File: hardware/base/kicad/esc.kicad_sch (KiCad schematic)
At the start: 69 parts, among them J3 HY911105AE IN, J4 HY911105AE OUT, U4 LAN9253-I/R4X, U5 TPS3808G33DBVR, U6 M24C16-RMN6TP, U7 TPD4E05U06DQAR, U8 TPD4E05U06DQAR

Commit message: Place the base board parts; DIP switches for the encoder terminations
Placement (gen/pcb.py): one zone per schematic sheet, key parts placed by
hand, the other parts next to the pin they serve, bulkiest first, with a
1 mm gap preferred when it costs at most 2 mm. The local bus header stands
at the left end, centred across the board, facing the modules.

Encoder terminations: one CTS 218-4LPSTR DIP switch per encoder (100 mA
non-switching) replaces three SMD jumpers; the supply selector and the
Modbus termination use a through-hole 1x3 header. Split DIP symbol, one
unit per switch, drawn on the pair it serves.

DRC rules: 0.2 mm thermal vias, per-package clearance for 0.65 mm pitch
parts. Test points out of the BOM, DNP copied to the footprints. pcb.py
keeps the schematic settings of the project file and finds the KiCad
footprint libraries on every install.

Claude-Session: https://claude.ai/code/session_01JfmMsHNpEd1mfzHNWc4koJ
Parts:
- TP1, TP2, TP3: now left out of the parts list

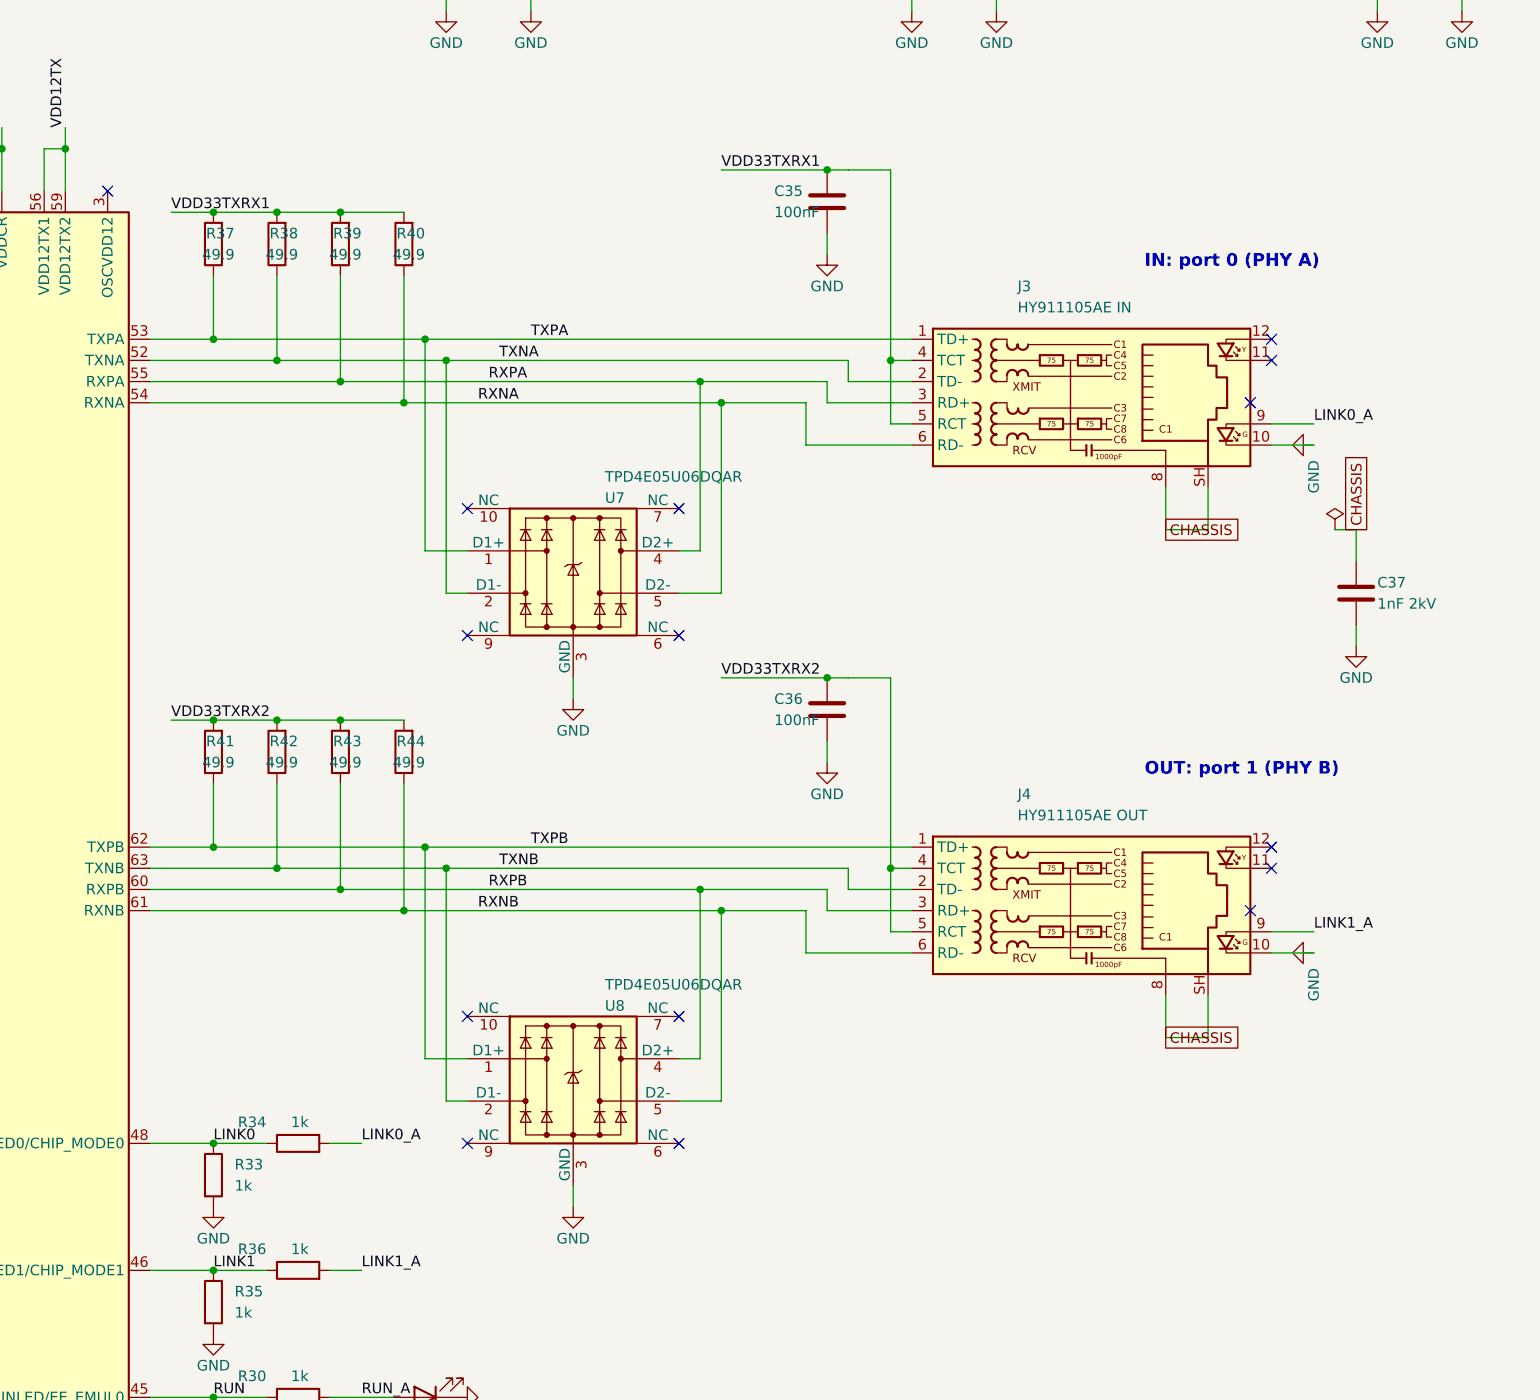
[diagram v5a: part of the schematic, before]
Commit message: Differential pairs routed by script; PHY to jack mapping for a planar layout
- pairs.py, pass "pairs" right after the planes and trunks: A* on a 0.1 mm
  grid for the centre line of each pair, clear of the other copper by about
  3 W (by the clearance alone near the pads), offset into its two lines;
  straight out of the QFN pads, straight through the ESD arrays, each line on
  its own into the through-hole pins of the jack. Ethernet 100 ohm and USB
  90 ohm at 0.15 mm gap (sim/impedance.py).
- Schematic: the lines on the jack pins and ESD channels in the order that
  routes without a crossing (port A with P and N swapped, port B with TX and
  RX swapped: the LAN9253 PHYs correct the polarity and have HP Auto-MDIX);
  the NC pins of the ESD arrays opposite each line carry it (TI flow-through).
- Ethernet terminations lifted off the board while the pairs are routed, then
  put against their line, 2 to 10 mm from the PHY pins; the lines inside a
  port straddled by their 0603 termination (49.9 ohm moved to 0603, C23185,
  basic, 1.78 M in stock on 2026-10-20; clock series resistors too).
- Placement: lanes of the pairs kept free of other parts (LAN9253 checklist);
  ESD arrays in the way of their lines; centre tap capacitors at the jacks;
  VDD33TXRX mini-planes in layer 3 under the terminations.
- route.py: real C-LOCK cutout clearance for copper; via hole to pad
  clearance; mini-plane priority in the plane test.
- kicadgen: tagged labels do not name a net (a second label on a NC pin).

Claude-Session: https://claude.ai/code/session_01D6Na26JP4CWdxCU6BKa4Yc
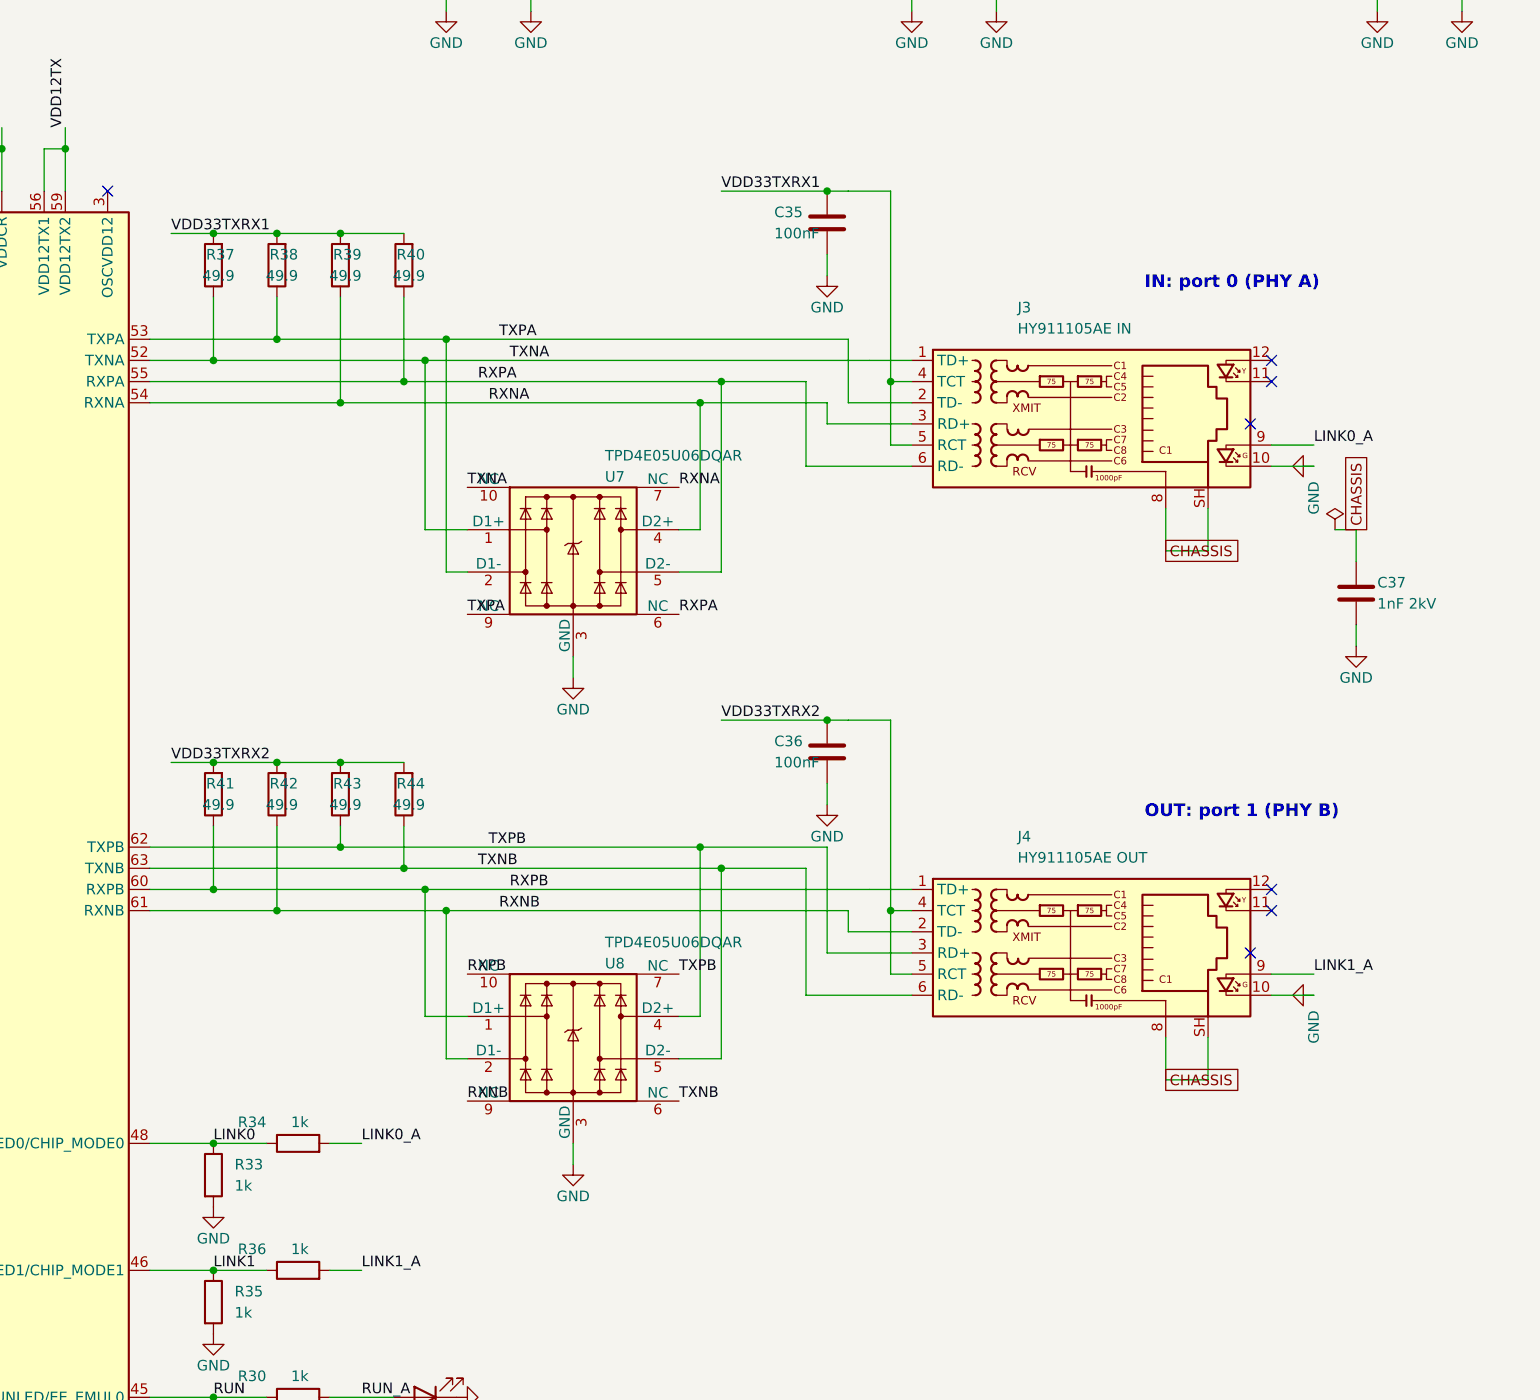
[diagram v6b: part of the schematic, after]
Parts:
- R37, R38, R39, R40, R41, R42, R43, R44: footprint Resistor_SMD:R_0402_1005Metric -> Resistor_SMD:R_0603_1608Metric; LCSC C25120 -> C23185
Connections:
- net RXNA: now also J3.3 (RD+), R39.1, U7.4 (D2+), U7.7 (NC); no longer J3.6 (RD-), R40.1, U7.5 (D2-)
- net RXNB: now also J4.2 (TD-), R42.1, U8.2 (D1-), U8.9 (NC); no longer J4.6 (RD-), R44.1, U8.5 (D2-)
- net RXPA: now also J3.6 (RD-), R40.1, U7.5 (D2-), U7.6 (NC); no longer J3.3 (RD+), R39.1, U7.4 (D2+)
- net RXPB: now also J4.1 (TD+), R41.1, U8.1 (D1+), U8.10 (NC); no longer J4.3 (RD+), R43.1, U8.4 (D2+)
- net TXNA: now also J3.1 (TD+), R37.1, U7.1 (D1+), U7.10 (NC); no longer J3.2 (TD-), R38.1, U7.2 (D1-)
- net TXNB: now also J4.6 (RD-), R44.1, U8.5 (D2-), U8.6 (NC); no longer J4.2 (TD-), R42.1, U8.2 (D1-)
- net TXPA: now also J3.2 (TD-), R38.1, U7.2 (D1-), U7.9 (NC); no longer J3.1 (TD+), R37.1, U7.1 (D1+)
- net TXPB: now also J4.3 (RD+), R43.1, U8.4 (D2+), U8.7 (NC); no longer J4.1 (TD+), R41.1, U8.1 (D1+)
- no-connect marks 37 -> 29
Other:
- moved on the sheet: C35, C36, J3, J4, R37, R38, R39, R40, R41, R42, R43, R44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
